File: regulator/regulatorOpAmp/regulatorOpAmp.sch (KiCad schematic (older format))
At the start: 8 parts, among them U1 AD822A

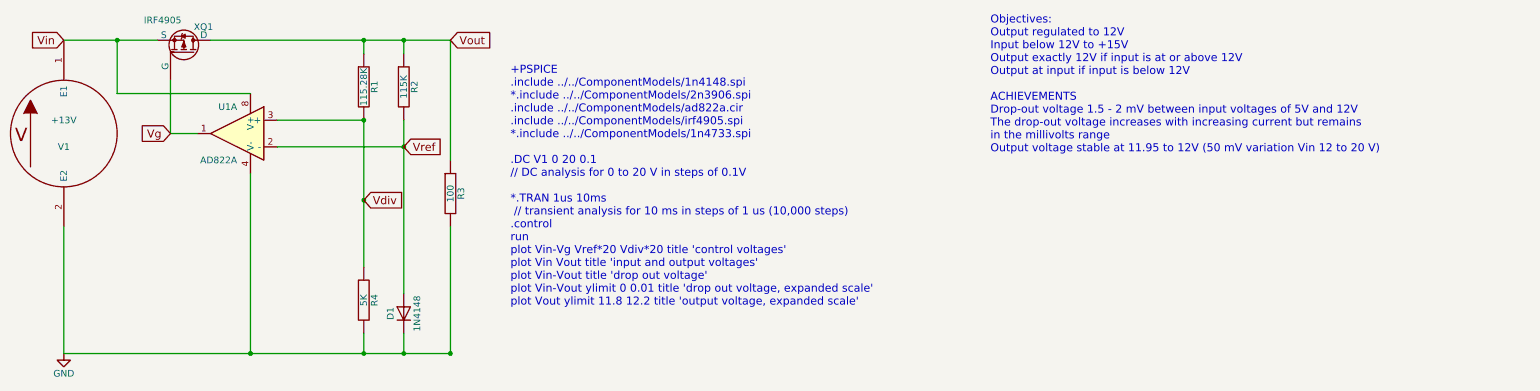
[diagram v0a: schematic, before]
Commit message: update for 1 and 2 amp current
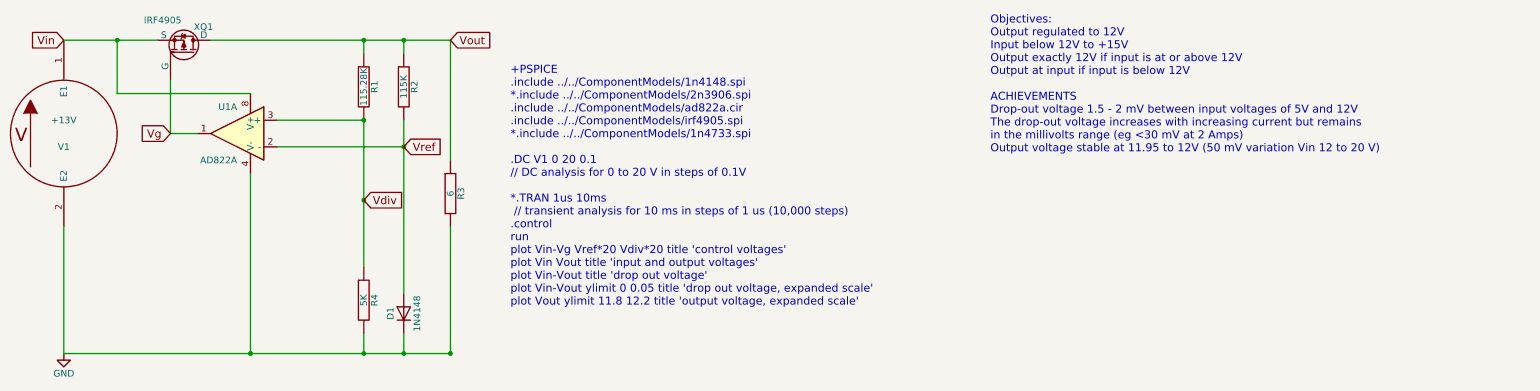
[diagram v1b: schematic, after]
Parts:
- R3: value 100 -> 6
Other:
- note added: "Objectives:\nOutput regulated to 12V\nInput below 12V to +15V\nOutput exactly 12V if input is at or above 12V\nOutput at input if input is below 12V\n\nACHIEVEMENTS\nDrop-out voltage 1.5 - 2 mV between input voltages of 5V and 12V\nThe drop-out voltage increases with increasing current but remains \nin the millivolts range (eg <30 mV at 2 Amps)\nOutput voltage stable at 11.95 to 12V (50 mV variat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"
- note removed: "Objectives:\nOutput regulated to 12V\nInput below 12V to +15V\nOutput exactly 12V if input is at or above 12V\nOutput at input if input is below 12V\n\nACHIEVEMENTS\nDrop-out voltage 1.5 - 2 mV between input voltages of 5V and 12V\nThe drop-out voltage increases with increasing current but remains \nin the millivolts range\nOutput voltage stable at 11.95 to 12V (50 mV variation Vin 12 to 20 V)"
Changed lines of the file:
@@
 $EndComp
 Text Notes 4250 2700 0    60   ~ 0
-+PSPICE \n.include ../../ComponentModels/1n4148.spi\n*.include ../../ComponentModels/2n3906.spi\n.include ../../ComponentModels/ad822a.cir\n.include ../../ComponentModels/irf4905.spi\n*.include ../../ComponentModels/1n4733.spi\n\n.DC V1 0 20 0.1  \n// DC analysis for 0 to 20 V in steps of 0.1V \n\n*.TRAN 1us 10ms\n // transient analysis for 10 ms in steps of 1 us (10,000 steps)\n.control\nrun\nplot Vin-Vg Vref*20 Vdiv*20 title 'control voltages'\nplot Vin Vout title 'input and output voltages'\nplot Vin-Vout title 'drop out voltage'\nplot Vin-Vout ylimit 0 0.01 title 'drop out voltage, expanded scale'\nplot Vout ylimit 11.8 12.2 title 'output voltage, expanded scale'\n
++PSPICE \n.include ../../ComponentModels/1n4148.spi\n*.include ../../ComponentModels/2n3906.spi\n.include ../../ComponentModels/ad822a.cir\n.include ../../ComponentModels/irf4905.spi\n*.include ../../ComponentModels/1n4733.spi\n\n.DC V1 0 20 0.1  \n// DC analysis for 0 to 20 V in steps of 0.1V \n\n*.TRAN 1us 10ms\n // transient analysis for 10 ms in steps of 1 us (10,000 steps)\n.control\nrun\nplot Vin-Vg Vref*20 Vdiv*20 title 'control voltages'\nplot Vin Vout title 'input and output voltages'\nplot Vin-Vout title 'drop out voltage'\nplot Vin-Vout ylimit 0 0.05 title 'drop out voltage, expanded scale'\nplot Vout ylimit 11.8 12.2 title 'output voltage, expanded scale'\n
 $Comp
 L VSOURCE V1
@@
 	3800 3050 3800 2100
 Text Notes 7850 1550 0    60   ~ 0
-Objectives:\nOutput regulated to 12V\nInput below 12V to +15V\nOutput exactly 12V if input is at or above 12V\nOutput at input if input is below 12V\n\nACHIEVEMENTS\nDrop-out voltage 1.5 - 2 mV between input voltages of 5V and 12V\nThe drop-out voltage increases with increasing current but remains \nin the millivolts range\nOutput voltage stable at 11.95 to 12V (50 mV variation Vin 12 to 20 V)
+Objectives:\nOutput regulated to 12V\nInput below 12V to +15V\nOutput exactly 12V if input is at or above 12V\nOutput at input if input is below 12V\n\nACHIEVEMENTS\nDrop-out voltage 1.5 - 2 mV between input voltages of 5V and 12V\nThe drop-out voltage increases with increasing current but remains \nin the millivolts range (eg <30 mV at 2 Amps)\nOutput voltage stable at 11.95 to 12V (50 mV variation Vin 12 to 20 V)
 Connection ~ 3800 3050
 Wire Wire Line
@@
 P 3800 1850
 F 0 "R3" V 3880 1850 50  0000 C CNN
-F 1 "100" V 3800 1850 50  0000 C CNN
+F 1 "6" V 3800 1850 50  0000 C CNN
 F 2 "" H 3800 1850 50  0001 C CNN
 F 3 "" H 3800 1850 50  0001 C CNN
